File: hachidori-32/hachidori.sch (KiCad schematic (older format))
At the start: 43 parts, among them P1 VIN, P2 UART, SW1 FLASH, SW2 RESET, U1 ADP3338, U2 MPU-9250, U4 BME280, U7 INA226

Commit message: Annotated
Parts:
- gave numbers to parts that had none: 13
- renumbered CB10 to CB1, CB1 to CB2, CB11 to CB3, CB2 to CB4, CB3 to CB6, CB4 to CB7, CB6 to CB8, P2 to P9, R26 to R1, R7 to R11, R27 to R2, R25 to R3, R1 to R4, R9 to R5, R10 to R6, R4 to R7, SW2 to SW1, SW1 to SW2, TH2 to TH1, TH3 to TH2, U7 to U2, U2 to U4, U4 to U5

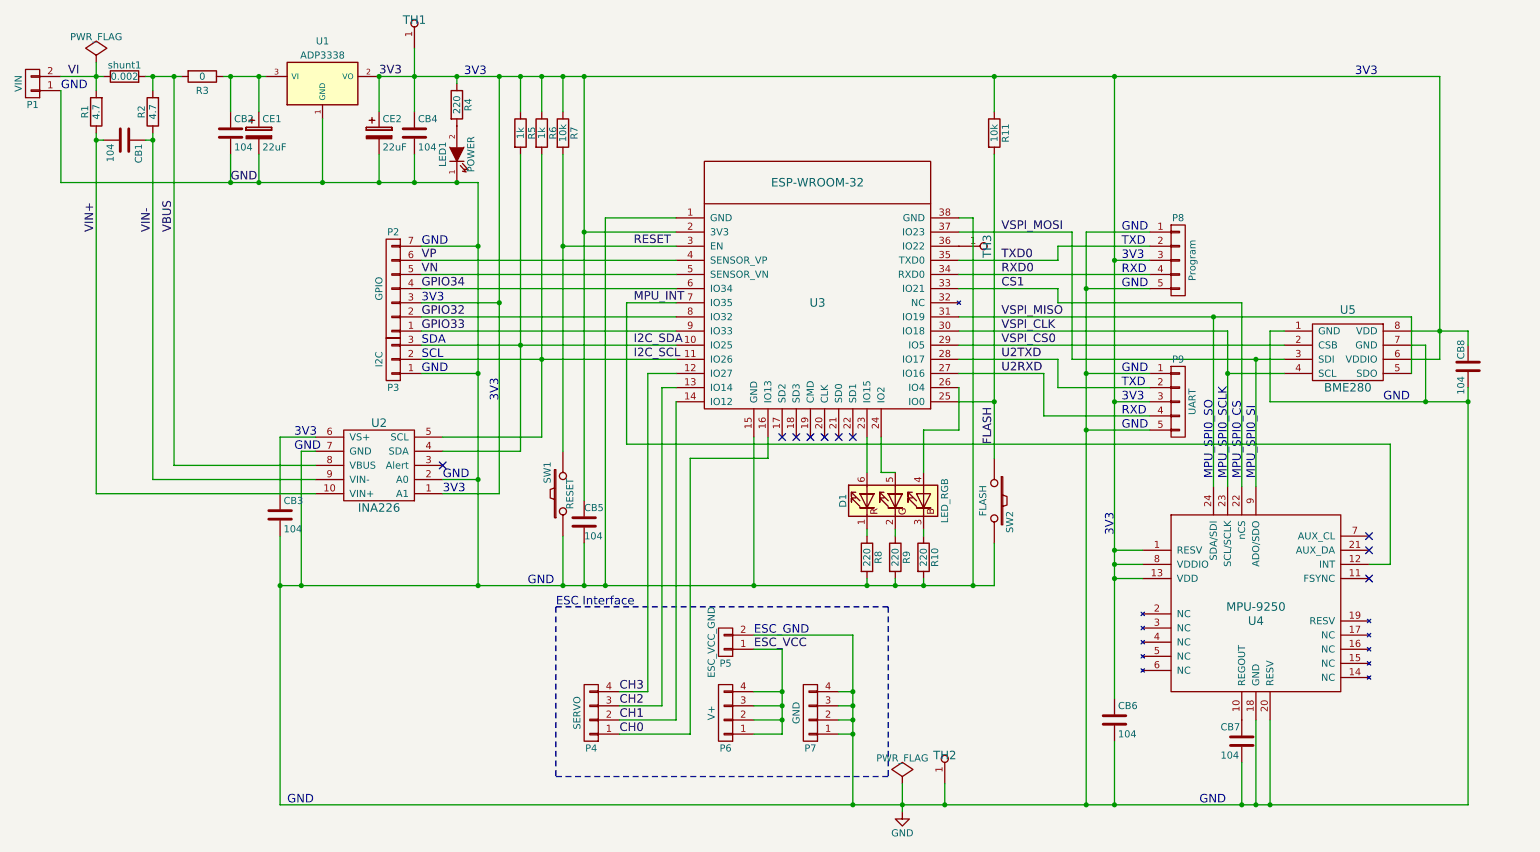
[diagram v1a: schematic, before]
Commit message: Add LEDs for identification
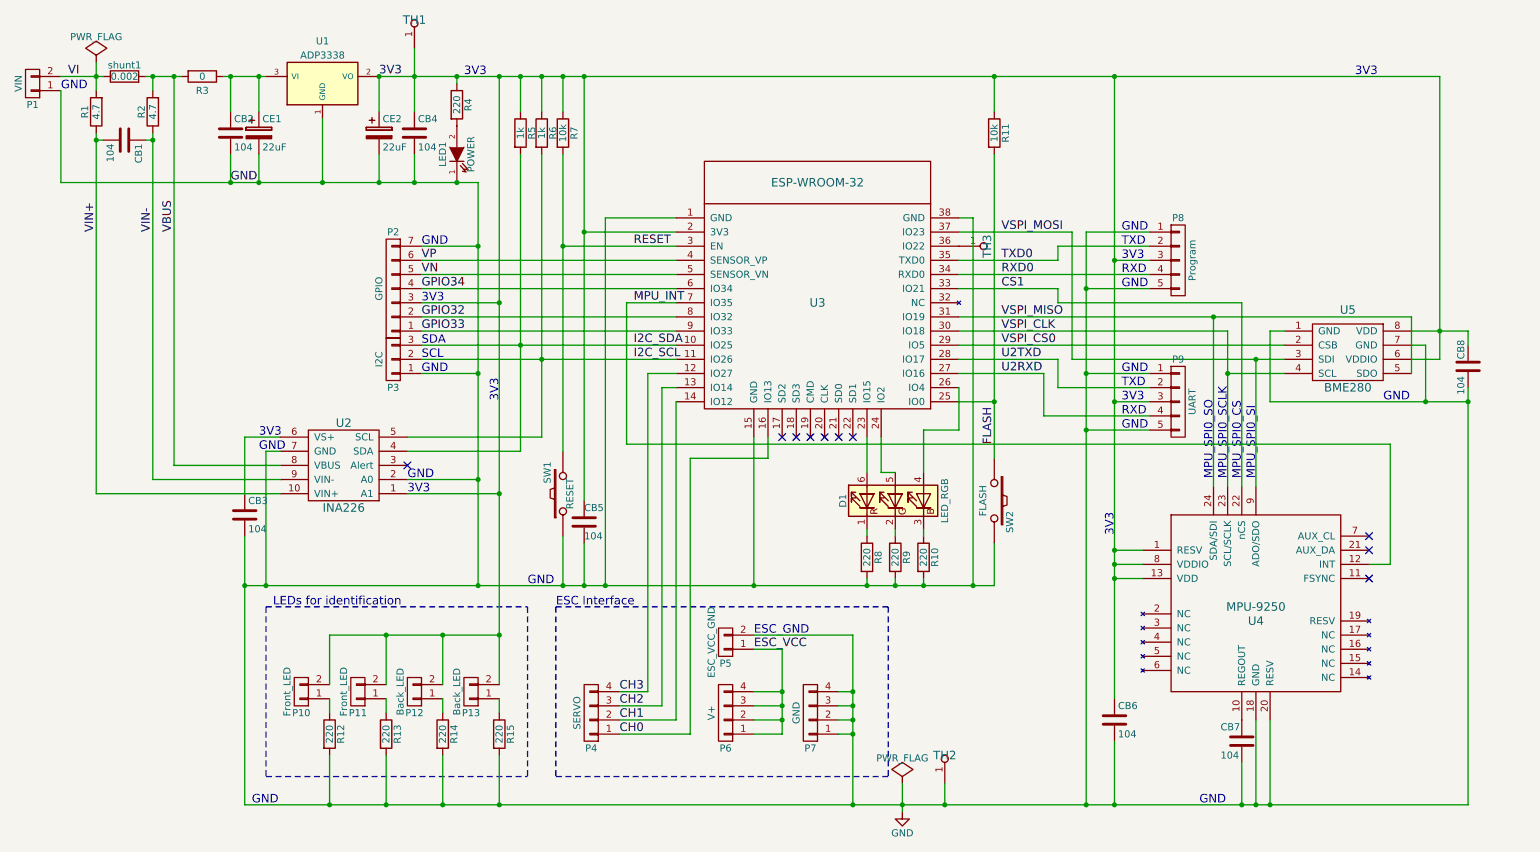
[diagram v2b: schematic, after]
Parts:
- added P10, P11: Front_LED, symbol CONN_01X02
- added P12, P13: Back_LED, symbol CONN_01X02
- added R12, R13, R14, R15: 220, rohm:MCR03, symbol R
- P2: footprint (none) -> droneworks:Pin_Header_1x07
- P3: footprint (none) -> droneworks:Pin_Header_1x03
- U3: footprint (none) -> droneworks:ESP32-WROOM
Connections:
- net 3V3: now also P10.2 (P2), P11.2 (P2), P12.2 (P2), P13.2 (P2)
- net GND: now also R12.2, R13.2, R14.2, R15.2
- new net: P10.1 (P1), R12.1
- new net: P12.1 (P1), R14.1
- new net: P11.1 (P1), R13.1
- new net: P13.1 (P1), R15.1
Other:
- note added: "LEDs for identification"
- moved on the sheet: CB3, U2

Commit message: allocated footprint
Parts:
- P10, P11, P12, P13: footprint (none) -> droneworks:Pin_Header_1x02
- shunt1: footprint rohm:MCR03 -> rohm:PMR18

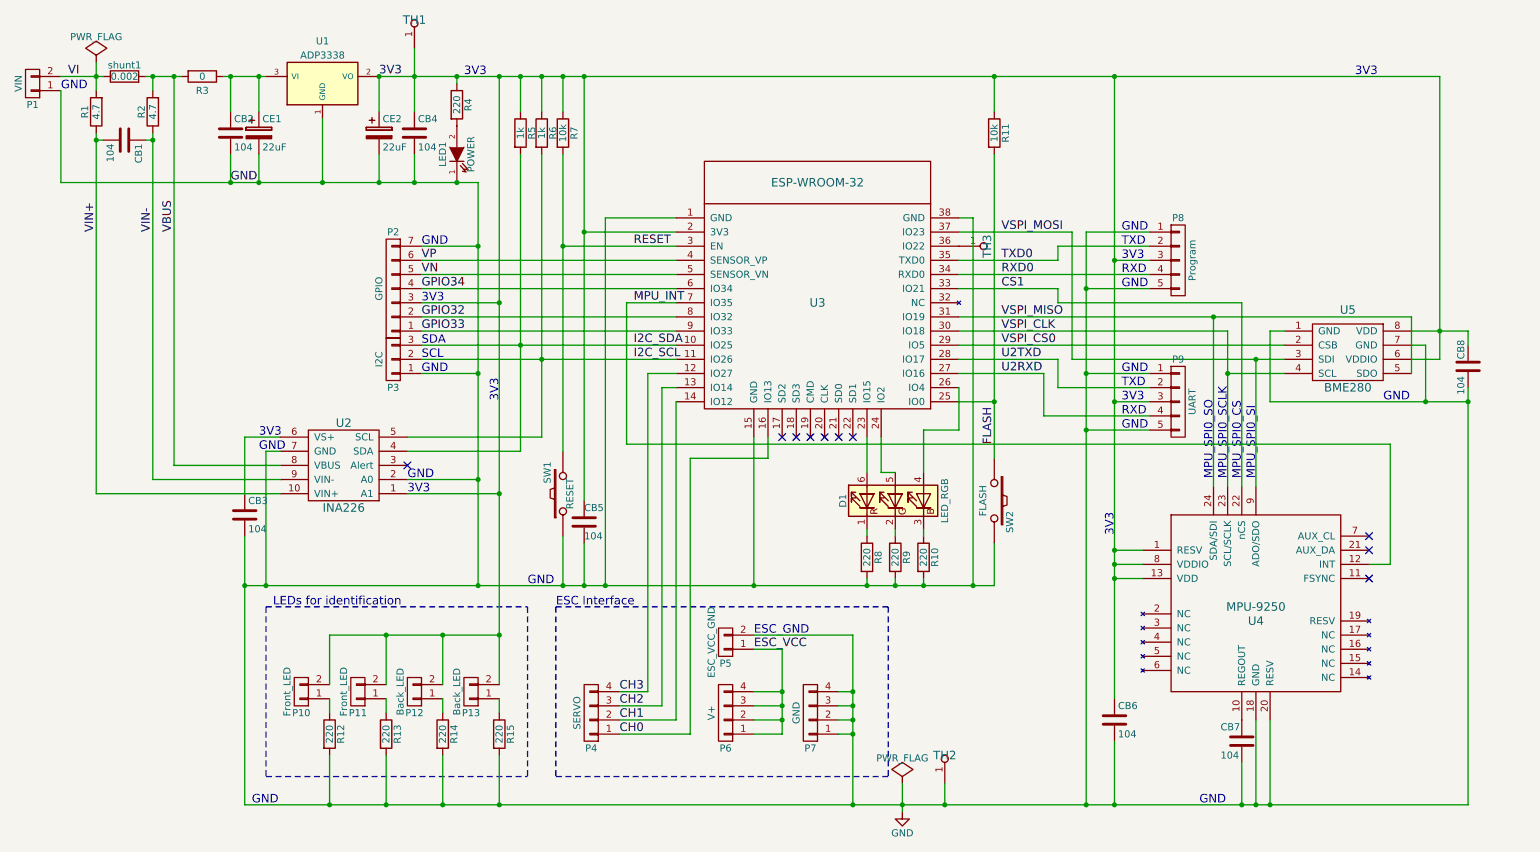
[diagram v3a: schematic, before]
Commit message: fix RGB_LED
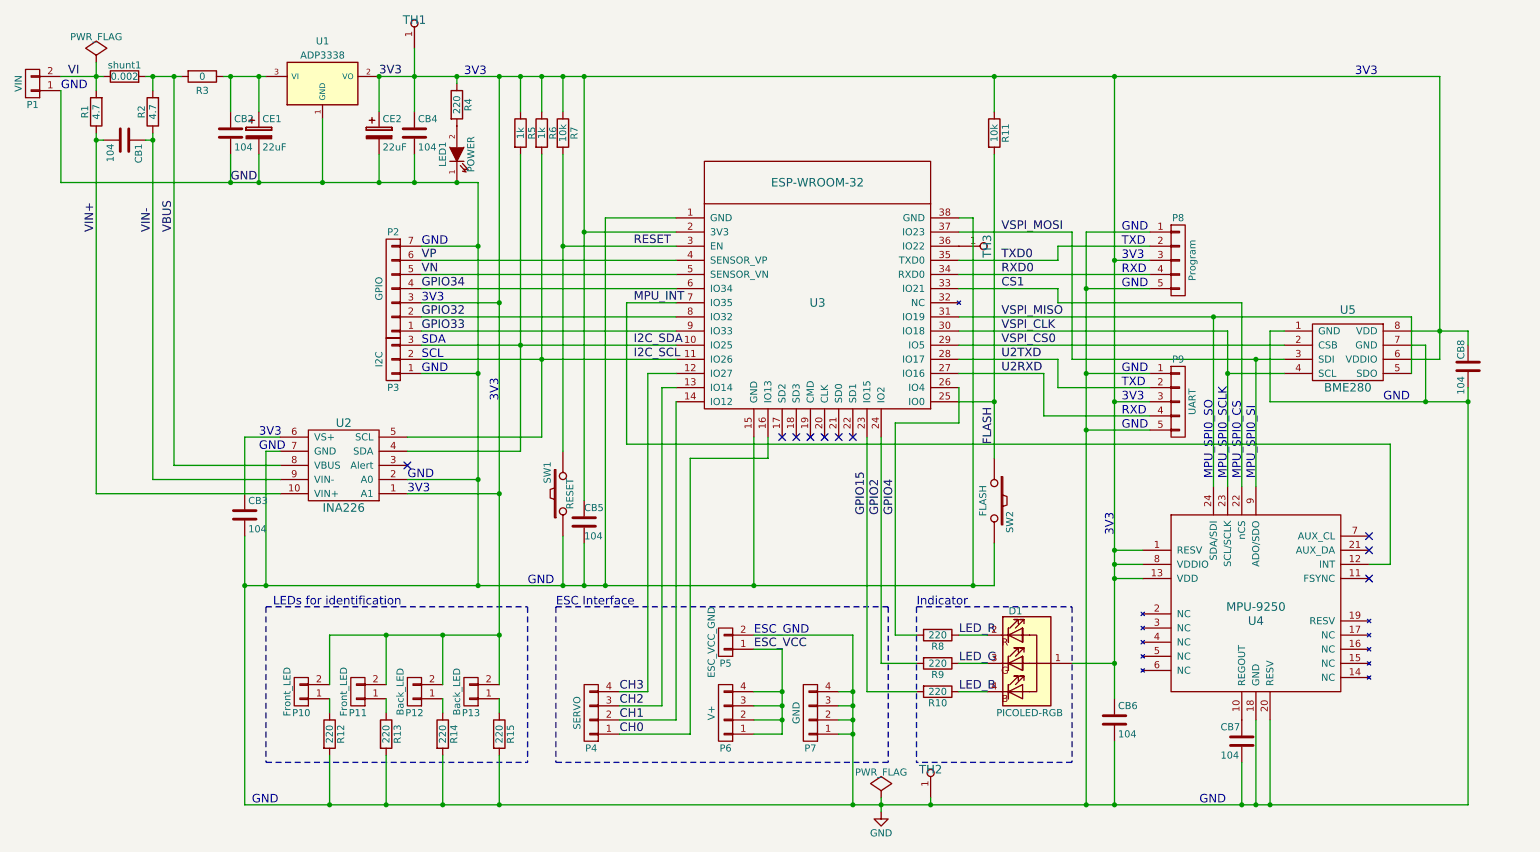
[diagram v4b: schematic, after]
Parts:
- removed D1: LED_RGB, symbol LED_RGB
- added D1: PICOLED-RGB, rohm:SMLP34RGB, symbol PICOLED-RGB
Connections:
- net 3V3: now also D1.1 (Anode)
- net GND: no longer R10.2, R8.2, R9.2
- net GPIO15: now reaches U3.23 (IO15)
- net GPIO15: now also R10.2
- net GPIO2: now reaches U3.24 (IO2)
- net GPIO2: now also R9.2
- net GPIO4: now reaches U3.26 (IO4)
- net GPIO4: now also R8.2
- net LED_R: now reaches R8.1
- net LED_R: now also D1.2 (RK)
- net LED_G: now reaches R9.1
- net LED_G: now also D1.3 (GK)
- net LED_B: now reaches R10.1
- net LED_B: now also D1.4 (BK)
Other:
- note added: "Indicator"
- moved on the sheet: R10, R8, R9, TH2
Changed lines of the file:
@@
 Sheet 1 1
 Title "hachidori-32"
-Date "2017-02-16"
-Rev "0.08"
+Date "2017-02-17"
+Rev "0.09"
 Comp ""
 Comment1 "Copyright (c) 2017 DroneWorks Inc."
@@
 L PWR_FLAG #FLG02
 U 1 1 57BB513D
-P 6850 6350
-F 0 "#FLG02" H 6850 6445 50  0001 C CNN
-F 1 "PWR_FLAG" H 6850 6530 50  0000 C CNN
-F 2 "" H 6850 6350 50  0000 C CNN
-F 3 "" H 6850 6350 50  0000 C CNN
-	1    6850 6350
+P 6700 6450
+F 0 "#FLG02" H 6700 6545 50  0001 C CNN
+F 1 "PWR_FLAG" H 6700 6630 50  0000 C CNN
+F 2 "" H 6700 6450 50  0000 C CNN
+F 3 "" H 6700 6450 50  0000 C CNN
+	1    6700 6450
 	1    0    0    -1
 $EndComp
@@
 L GND #PWR03
 U 1 1 57BB5D93
-P 6850 6550
-F 0 "#PWR03" H 6850 6300 50  0001 C CNN
-F 1 "GND" H 6850 6400 50  0000 C CNN
-F 2 "" H 6850 6550 50  0000 C CNN
-F 3 "" H 6850 6550 50  0000 C CNN
-	1    6850 6550
+P 6700 6550
+F 0 "#PWR03" H 6700 6300 50  0001 C CNN
+F 1 "GND" H 6700 6400 50  0000 C CNN
+F 2 "" H 6700 6550 50  0000 C CNN
+F 3 "" H 6700 6550 50  0000 C CNN
+	1    6700 6550
 	1    0    0    -1
 $EndComp
@@
 L throughhole TH2
 U 1 1 57FAF6F8
-P 7150 6350
-F 0 "TH2" H 7150 6150 60  0000 C CNN
-F 1 "GND" H 7250 6500 60  0001 C CNN
-F 2 "droneworks:TH" V 7150 6350 60  0001 C CNN
-F 3 "" H 7150 6350 60  0000 C CNN
-	1    7150 6350
+P 7050 6450
+F 0 "TH2" H 7050 6250 60  0000 C CNN
+F 1 "GND" H 7150 6600 60  0001 C CNN
+F 2 "droneworks:TH" V 7050 6450 60  0001 C CNN
+F 3 "" H 7050 6450 60  0000 C CNN
+	1    7050 6450
 	-1   0    0    1
 $EndComp
@@
 Text Notes 8400 3750 0    60   ~ 0
 RXD
-$Comp
-L ESP-WROOM-32 U3
-U 1 1 58A25DAF
-P 6250 2950
-F 0 "U3" H 6250 2950 60  0000 C CNN
-F 1 "ESP-WROOM-32" H 6250 3800 60  0000 C CNN
-F 2 "droneworks:ESP32-WROOM" H 6250 2950 60  0001 C CNN
-F 3 "" H 6250 2950 60  0001 C CNN
-	1    6250 2950
-	1    0    0    -1
-$EndComp
 NoConn ~ 6000 3900
 NoConn ~ 6100 3900
@@
 MPU_INT
 $Comp
-L LED_RGB D1
-U 1 1 58A40043
-P 6800 4350
-F 0 "D1" H 6800 4720 50  0000 C CNN
-F 1 "LED_RGB" H 6800 4000 50  0000 C CNN
-F 2 "" H 6800 4300 50  0001 C CNN
-F 3 "" H 6800 4300 50  0000 C CNN
-	1    6800 4350
-	0    -1   -1   0
-$EndComp
-$Comp
 L R R8
 U 1 1 58A40751
-P 6600 4750
-F 0 "R8" V 6680 4750 50  0000 C CNN
-F 1 "220" V 6600 4750 50  0000 C CNN
-F 2 "rohm:MCR03" V 6530 4750 50  0001 C CNN
-F 3 "" H 6600 4750 50  0000 C CNN
-	1    6600 4750
-	1    0    0    -1
+P 7100 5300
+F 0 "R8" V 7180 5300 50  0000 C CNN
+F 1 "220" V 7100 5300 50  0000 C CNN
+F 2 "rohm:MCR03" V 7030 5300 50  0001 C CNN
+F 3 "" H 7100 5300 50  0000 C CNN
+	1    7100 5300
+	0    1    1    0
 $EndComp
 $Comp
 L R R9
 U 1 1 58A41D4E
-P 6800 4750
-F 0 "R9" V 6880 4750 50  0000 C CNN
-F 1 "220" V 6800 4750 50  0000 C CNN
-F 2 "rohm:MCR03" V 6730 4750 50  0001 C CNN
-F 3 "" H 6800 4750 50  0000 C CNN
-	1    6800 4750
-	1    0    0    -1
+P 7100 5500
+F 0 "R9" V 7180 5500 50  0000 C CNN
+F 1 "220" V 7100 5500 50  0000 C CNN
+F 2 "rohm:MCR03" V 7030 5500 50  0001 C CNN
+F 3 "" H 7100 5500 50  0000 C CNN
+	1    7100 5500
+	0    1    1    0
 $EndComp
 $Comp
 L R R10
 U 1 1 58A41DE5
-P 7000 4750
-F 0 "R10" V 7080 4750 50  0000 C CNN
-F 1 "220" V 7000 4750 50  0000 C CNN
-F 2 "rohm:MCR03" V 6930 4750 50  0001 C CNN
-F 3 "" H 7000 4750 50  0000 C CNN
-	1    7000 4750
-	1    0    0    -1
+P 7100 5700
+F 0 "R10" V 7180 5700 50  0000 C CNN
+F 1 "220" V 7100 5700 50  0000 C CNN
+F 2 "rohm:MCR03" V 7030 5700 50  0001 C CNN
+F 3 "" H 7100 5700 50  0000 C CNN
+	1    7100 5700
+	0    1    1    0
 $EndComp
 Wire Wire Line
@@
 Connection ~ 3850 3450
 Wire Wire Line
-	10850 3550 10850 6500
+	10850 6500 10850 3550
 Wire Wire Line
 	1200 1800 1150 1800
@@
 Connection ~ 10850 3650
 Wire Wire Line
-	6850 6350 6850 6550
-Connection ~ 6850 6500
+	6700 6450 6700 6550
+Connection ~ 6700 6500
 Connection ~ 8350 3650
 Wire Wire Line
@@
 	4400 5100 6750 5100
 Wire Notes Line
-	6750 5100 6750 6300
+	6750 5100 6750 6200
 Wire Wire Line
 	5900 3900 5900 4050
@@
 	5350 6000 4850 6000
 Wire Notes Line
-	4400 5100 4400 6300
+	4400 5100 4400 6200
 Wire Notes Line
-	4400 6300 6750 6300
+	4400 6200 6750 6200
 Wire Wire Line
 	7250 2750 8600 2750
@@
 Connection ~ 6500 6500
 Wire Wire Line
-	7150 6350 7150 6500
-Connection ~ 7150 6500
+	7050 6450 7050 6500
+Connection ~ 7050 6500
 Wire Wire Line
 	5800 4950 5800 3900
@@
 Wire Wire Line
 	10300 3950 10300 4800
-Wire Wire Line
-	6600 3900 6600 4150
-Wire Wire Line
-	6700 3900 6700 4150
-Wire Wire Line
-	6700 4150 6800 4150
-Wire Wire Line
-	7250 3550 7250 3850
-Wire Wire Line
-	6600 4600 6600 4550
-Wire Wire Line
-	6800 4600 6800 4550
-Wire Wire Line
-	7000 4600 7000 4550
-Wire Wire Line
-	7000 4900 7000 4950
-Connection ~ 7000 4950
-Wire Wire Line
-	6800 4900 6800 4950
-Connection ~ 6800 4950
-Wire Wire Line
-	6600 4900 6600 4950
-Connection ~ 6600 4950
-Wire Wire Line
-	7250 3850 7000 3850
-Wire Wire Line
-	7000 3850 7000 4150
 Wire Wire Line
 	5250 3150 3450 3150
@@
 LEDs for identification
 Wire Notes Line
-	2350 5100 2350 6300
+	2350 5100 2350 6200
 Wire Notes Line
-	2350 6300 4200 6300
+	2350 6200 4200 6200
 Wire Notes Line
 	2350 5100 4200 5100
 Wire Notes Line
-	4200 5100 4200 6300
+	4200 5100 4200 6200
+$Comp
+L PICOLED-RGB D1
+U 1 1 58A641CF
+P 7700 5500
+F 0 "D1" H 7650 5870 50  0000 C CNN
+F 1 "PICOLED-RGB" H 7750 5150 50  0000 C CNN
+F 2 "rohm:SMLP34RGB" H 7650 5450 50  0001 C CNN
+F 3 "" H 7650 5450 50  0000 C CNN
+	1    7700 5500
+	1    0    0    -1
+$EndComp
+$Comp
+L ESP-WROOM-32 U3
+U 1 1 58A25DAF
+P 6250 2950
+F 0 "U3" H 6250 2950 60  0000 C CNN
+F 1 "ESP-WROOM-32" H 6250 3800 60  0000 C CNN
+F 2 "droneworks:ESP32-WROOM" H 6250 2950 60  0001 C CNN
+F 3 "" H 6250 2950 60  0001 C CNN
+	1    6250 2950
+	1    0    0    -1
+$EndComp
+Wire Wire Line
+	6600 3900 6600 5700
+Wire Wire Line
+	6700 3900 6700 5500
+Wire Wire Line
+	8050 5500 8350 5500
+Connection ~ 8350 5500
+Wire Wire Line
+	6600 5700 6950 5700
+Wire Wire Line
+	6700 5500 6950 5500
+Wire Wire Line
+	7250 3550 7250 3800
+Wire Wire Line
+	7250 3800 6800 3800
+Wire Wire Line
+	6800 3800 6800 5300
+Wire Wire Line
+	6800 5300 6950 5300
+Wire Notes Line
+	6950 5100 6950 6200
+Wire Notes Line
+	8050 5100 8050 6200
+Wire Notes Line
+	6950 5100 8050 5100
+Wire Notes Line
+	8050 6200 6950 6200
+Text Notes 6950 5100 0    60   ~ 0
+Indicator
+Text Label 7250 5300 0    60   ~ 0
+LED_R
+Text Label 7250 5500 0    60   ~ 0
+LED_G
+Text Label 7250 5700 0    60   ~ 0
+LED_B
+Wire Wire Line
+	7250 5300 7450 5300
+Wire Wire Line
+	7250 5500 7450 5500
+Wire Wire Line
+	7250 5700 7450 5700
+Text Label 6800 4450 1    60   ~ 0
+GPIO4
+Text Label 6700 4450 1    60   ~ 0
+GPIO2
+Text Label 6600 4450 1    60   ~ 0
+GPIO15
 $EndSCHEMATC

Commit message: fix
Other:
- note added: "2SMPB-02A is\n Compatible with BME 280"
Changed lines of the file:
@@
 Title "hachidori-32"
 Date "2017-02-17"
-Rev "0.09"
+Rev "0.10"
 Comp ""
 Comment1 "Copyright (c) 2017 DroneWorks Inc."
@@
 Text Label 6600 4450 1    60   ~ 0
 GPIO15
+Text Notes 9600 2950 0    60   ~ 0
+2SMPB-02A is\n	 Compatible with BME 280
 $EndSCHEMATC

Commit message: fix and plot
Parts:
- U5: footprint droneworks:BME280 -> droneworks:campti_2SMPB-02A_BME280
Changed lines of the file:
@@
 Title "hachidori-32"
 Date "2017-02-17"
-Rev "0.10"
+Rev "0.11"
 Comp ""
 Comment1 "Copyright (c) 2017 DroneWorks Inc."
@@
 F 0 "U5" H 10000 3600 60  0000 C CNN
 F 1 "BME280" H 10000 3050 60  0000 C CNN
-F 2 "droneworks:BME280" H 10000 3250 60  0001 C CNN
+F 2 "droneworks:campti_2SMPB-02A_BME280" H 10000 3250 60  0001 C CNN
 F 3 "" H 10000 3250 60  0000 C CNN
 	1    10000 3300
